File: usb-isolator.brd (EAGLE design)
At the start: 30 x 30 mm, 23 parts, among them IC1 ADUM3160BRWZ

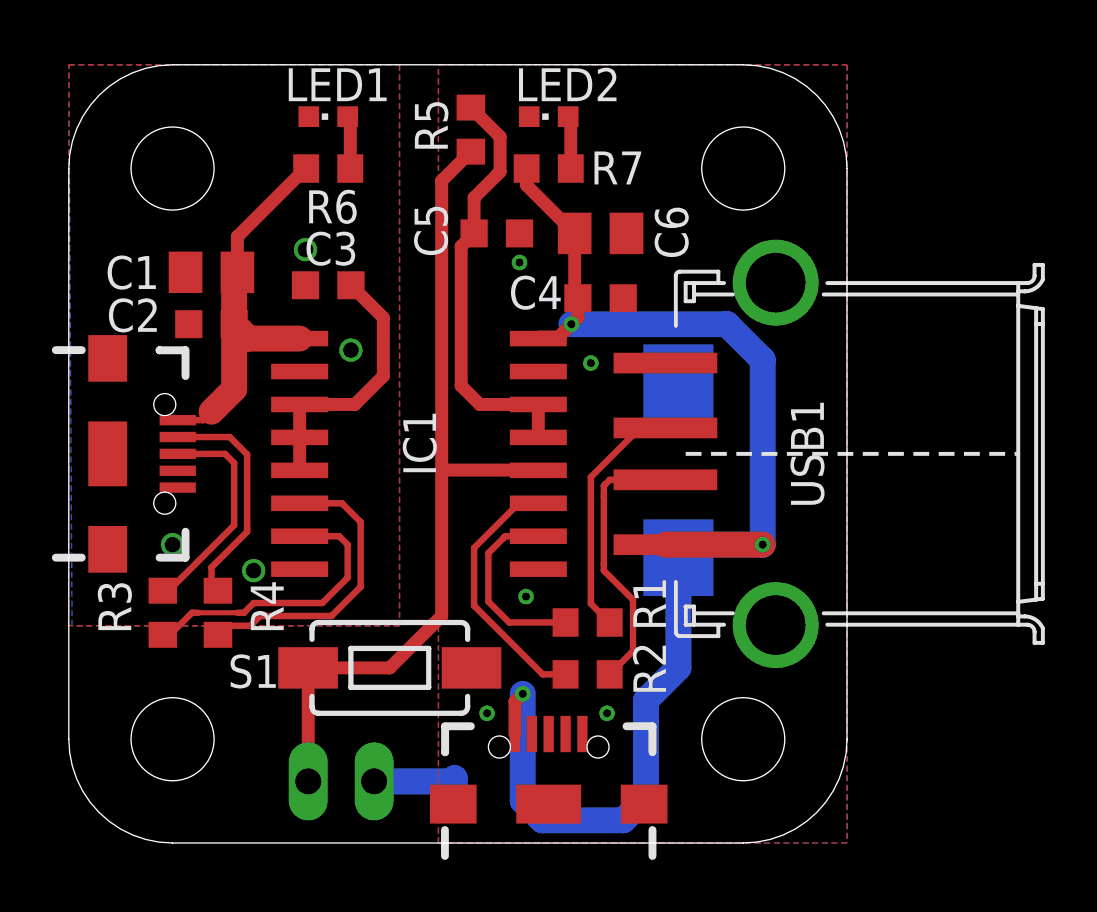
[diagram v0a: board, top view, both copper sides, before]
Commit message: Updated usb isolator 2 to move button, add slot
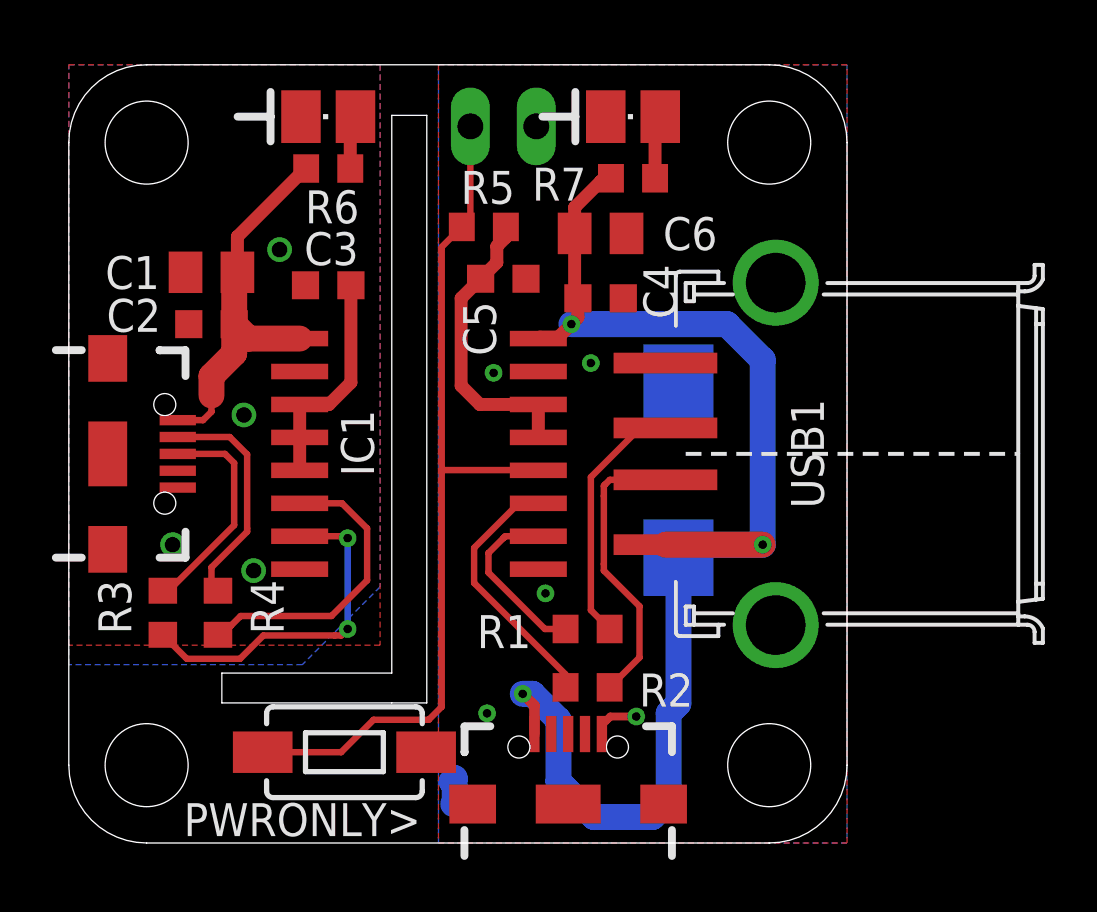
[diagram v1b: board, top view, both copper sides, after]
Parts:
- LED1, LED2: device semiconductors:LED-603 -> semiconductors:LED-805
- USB-ISOLATOR: value PCB_DP_SQUARE-3X3 -> PCB_DP_SQUARE-3X3V2; device mechanical:DP3030_V1 -> mechanical:DP3030_V2
- moved PIN 26.0 mm to (16.8, 27.6)
- moved R5 3.78 mm to (16.0, 23.8), turned to 0 degrees
- moved S1 3.69 mm to (10.6, 3.50)
- moved R7 3.27 mm to (21.8, 25.6)
- moved LED2 3.25 mm to (21.8, 28.0)
- moved C5 1.77 mm to (16.8, 21.8)
- moved J1 0.75 mm to (19.2, 1.50)
- moved R2 0.50 mm to (20.0, 6.00)
- moved R1 0.25 mm to (20.0, 8.25)
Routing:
- net VDD2: track 16.4 -> 11.4 mm
- net R_UD_P: track 11.3 -> 13.4 mm, vias 0 -> 2
- net PIN: track 32.4 -> 34.2 mm
- net VDD1: track 10.2 -> 9.00 mm
- net GND2: track 4.18 -> 3.01 mm
- net VBUS2: track 51.7 -> 50.8 mm
- net DD_N: track 10.6 -> 11.3 mm
- net N$13: track 2.04 -> 2.60 mm
- net R_DD_P: track 7.37 -> 6.82 mm
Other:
- outline, holes or cut-outs redrawn
- board text added: "CUT OUT"
- board text added: "PWRONLY>"
- board text added: "Tom Keddie USB Isolator v2.1"
- board text added: "o"
- board text removed: "Tom Keddie USB Isolator v2.0"
